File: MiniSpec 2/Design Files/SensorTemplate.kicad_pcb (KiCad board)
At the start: 2 copper layers, 14 x 25 mm, 1 part, among them J1 TSM-104-02-S-DV-P-TR

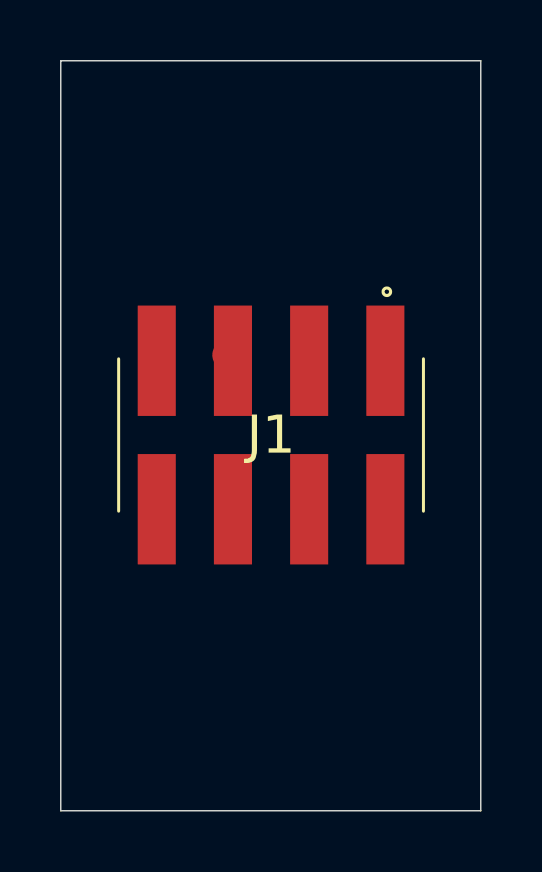
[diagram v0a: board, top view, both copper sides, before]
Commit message: added phone jack port for 25mm tube base
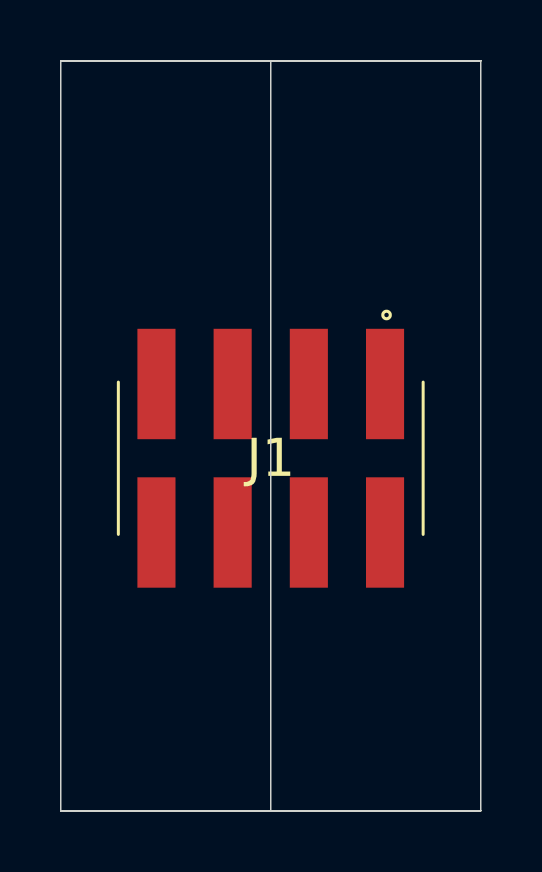
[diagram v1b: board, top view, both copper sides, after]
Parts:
- moved J1 0.78 mm to (145.0, 88.2)
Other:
- outline, holes or cut-outs redrawn
- net class Default removed
